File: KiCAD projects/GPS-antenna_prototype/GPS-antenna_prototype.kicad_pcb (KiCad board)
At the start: 2 copper layers, 71.1 x 134.6 mm, 1 part, among them J1 MMCX_Connector

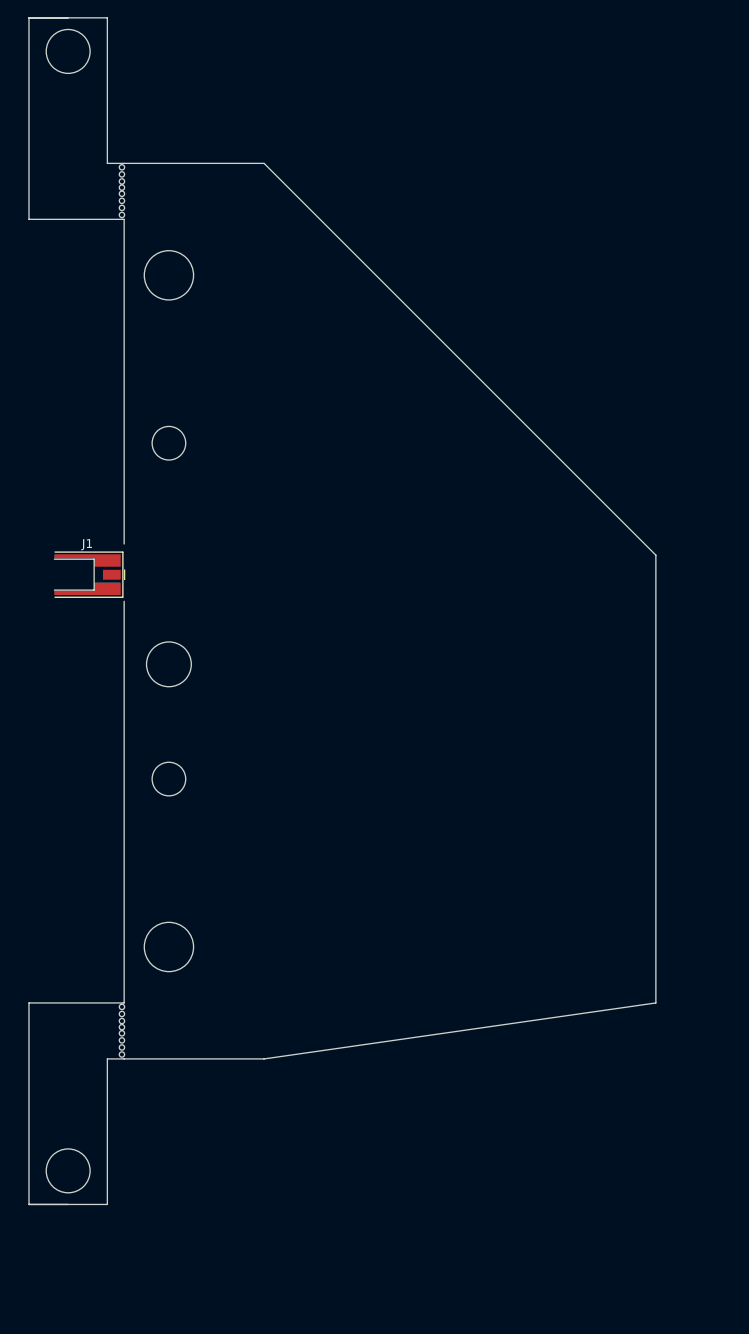
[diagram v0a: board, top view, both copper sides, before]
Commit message: Created KiCAD file for GPS Antenna
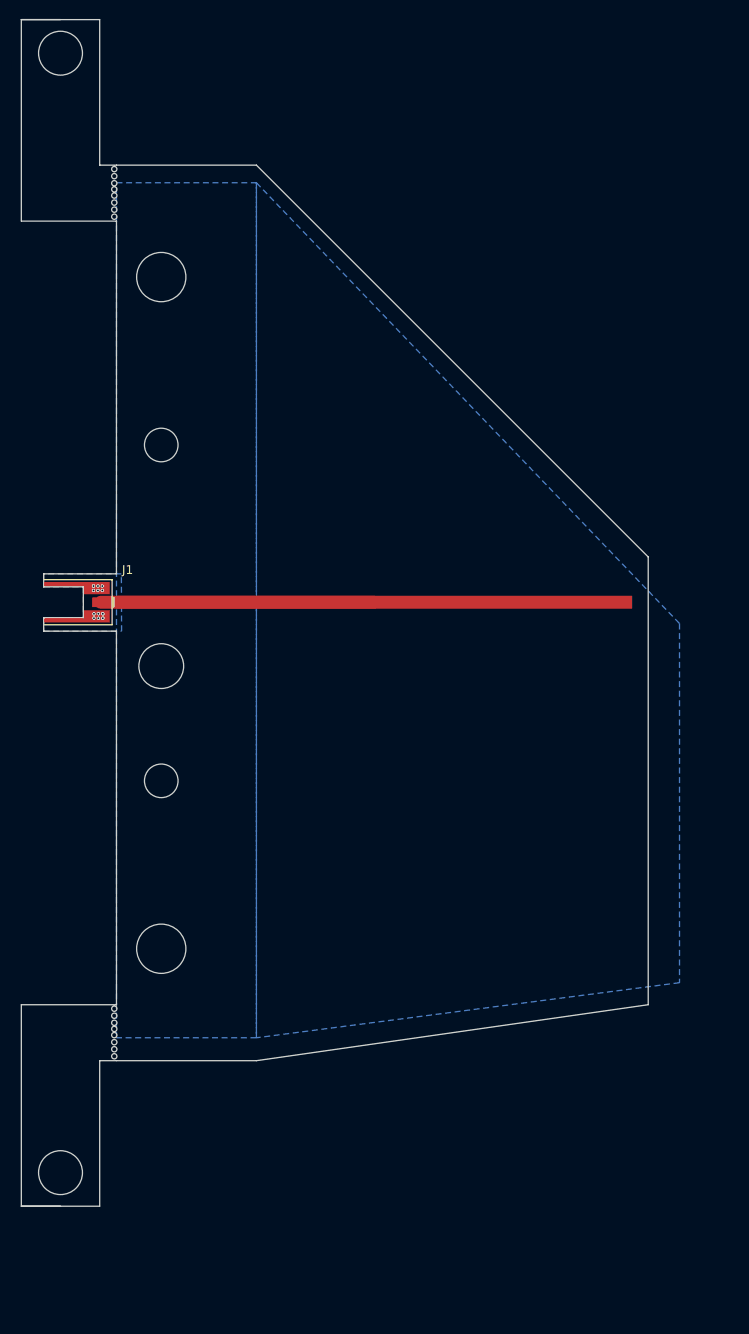
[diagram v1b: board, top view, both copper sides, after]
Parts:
- moved J1 3.36 mm to (80.3, 100.6)
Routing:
- net RadElement: track 0.00 -> 31.0 mm
- net GroundPlane: vias 0 -> 12
- added copper zone on B.Cu, net GroundPlane
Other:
- outline, holes or cut-outs redrawn

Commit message: finished creating production files
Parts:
- moved J1 0.44 mm to (80.0, 100.8)
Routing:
- net GroundPlane: track 0.00 -> 21.5 mm
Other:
- outline, holes or cut-outs redrawn

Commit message: PCB Changes
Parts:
- moved J1 1.61 mm to (80.0, 102.4)
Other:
- outline, holes or cut-outs redrawn

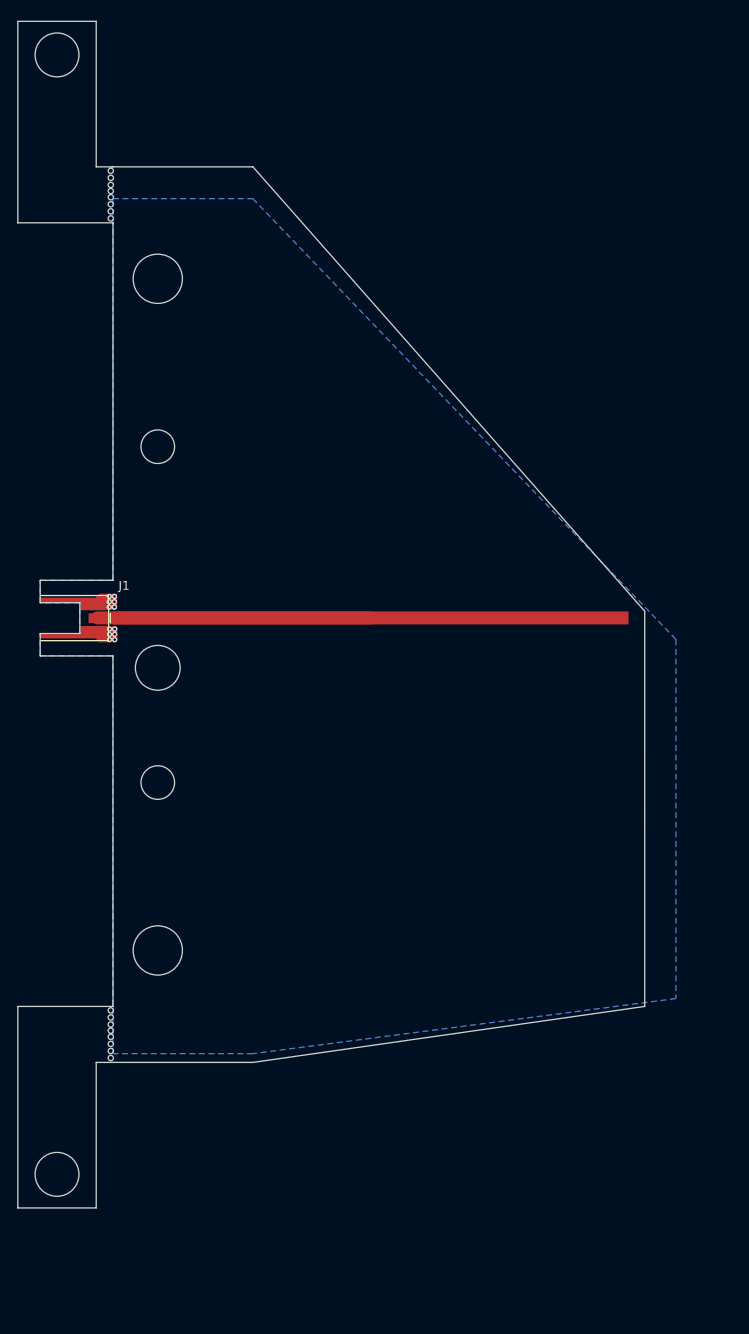
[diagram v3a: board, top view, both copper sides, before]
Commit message: Updated PCB files
The PCB files now have the more optimized geometry and reinforced mounting for production
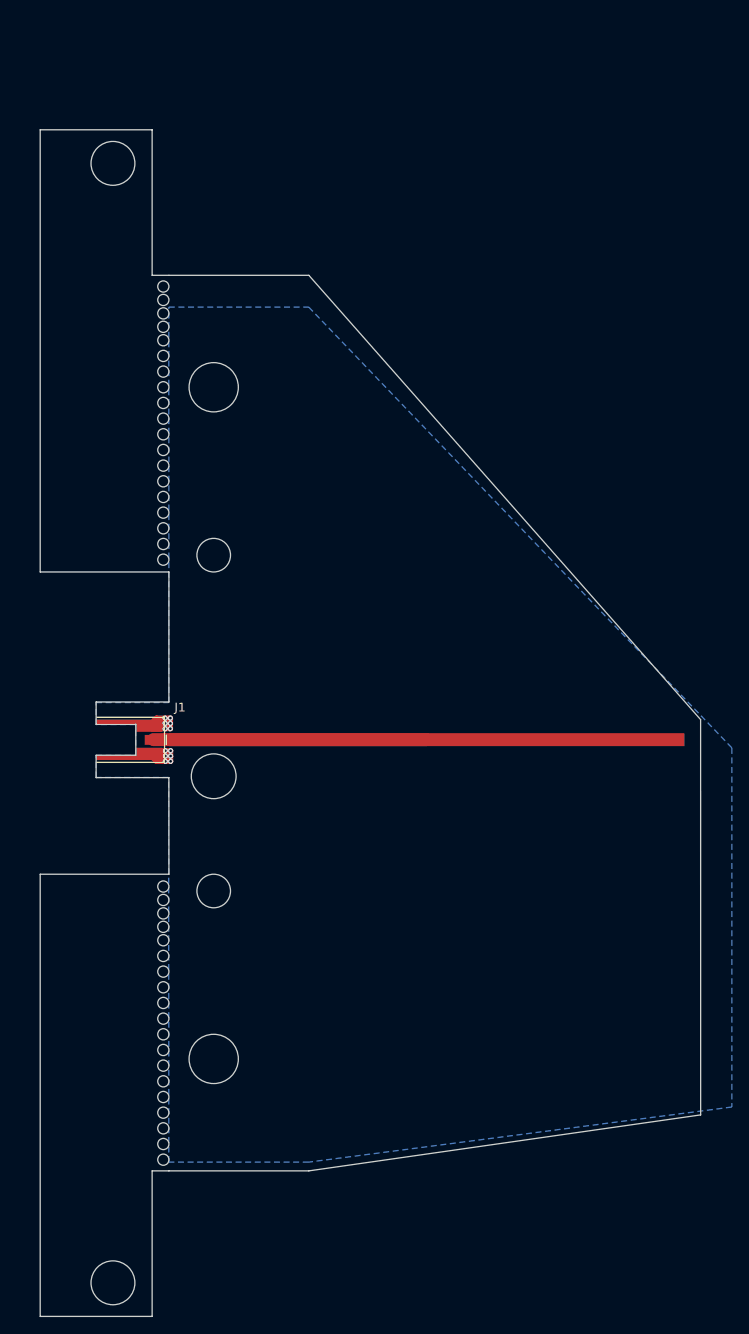
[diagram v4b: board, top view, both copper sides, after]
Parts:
- moved J1 15.2 mm to (86.3, 116.2)
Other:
- board size 71.1 x 134.6 mm -> 74.9 x 134.6 mm
